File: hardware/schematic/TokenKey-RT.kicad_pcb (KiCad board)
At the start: 4 copper layers, 50 x 40 mm, 103 parts, among them J1 USB-C, J2 Header 1x04 P2.54 H3.0 (OLED), J3 TC2030-NL, Q1 AO3401A, SW1 SW_BOOT, SW2 EC11E18244A5, SW3 BTN1, SW4 BTN2, U1 MIMXRT1062DVL6B, U2 AP2112K-3.3TRG1, U3 TLV62569DBVR, U4 W25Q64JVSSIQ, U5 APS6404L-3SQR-ZR, U6 USBLC6-2SC6, Y1 24MHz 12pF, Y2 32.768kHz 12.5pF

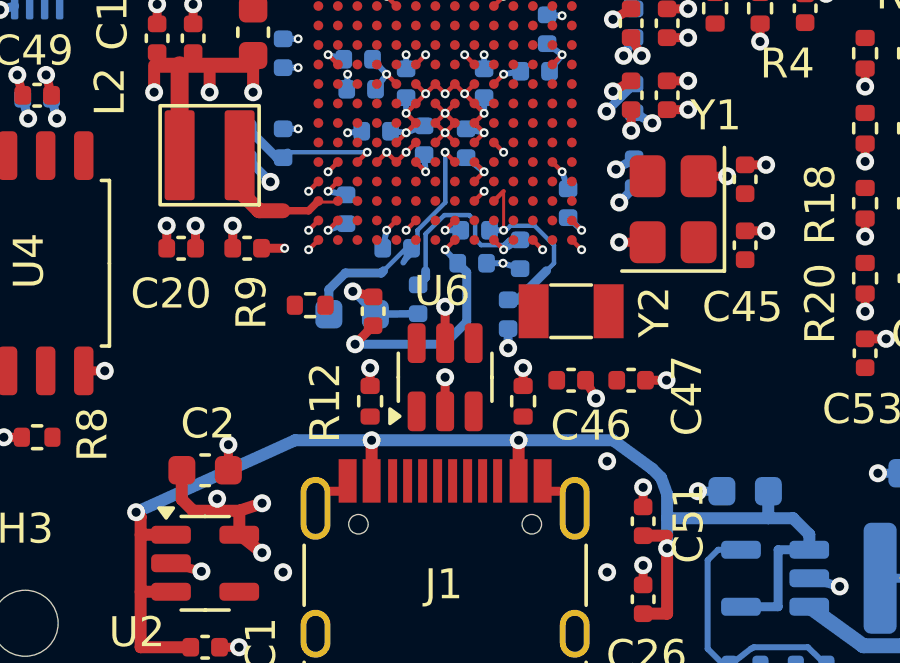
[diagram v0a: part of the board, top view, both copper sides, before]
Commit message: Route USB HS pair U1 -> USBLC6 -> J1 on L1 (Part of #58)
B-row J1 ties and diff-pair gap/uncoupled DRC errors remain open; see layout-notes §5.
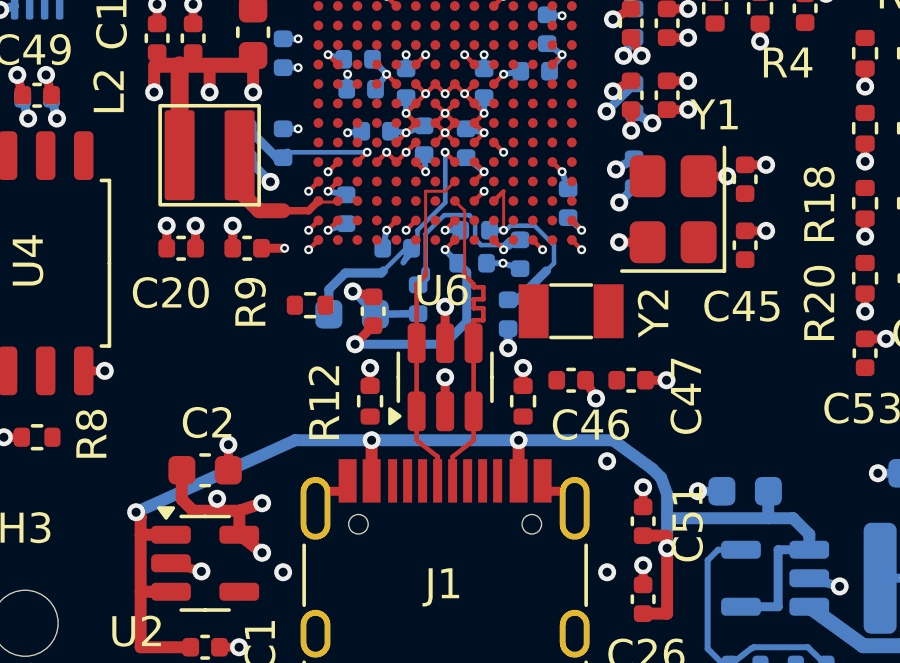
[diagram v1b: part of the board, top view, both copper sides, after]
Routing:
- net USB_DP: track 0.00 -> 11.2 mm
- net USB_DN: track 0.00 -> 11.2 mm
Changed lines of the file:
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@@
+	)
+	(segment
+		(start 16.05 30.4)
+		(end 16.05 30.9)
+		(width 0.155)
+		(layer "F.Cu")
+		(net 9)
+	)
+	(segment
+		(start 17 22.6)
+		(end 16.35 22.6)
+		(width 0.1)
+		(layer "F.Cu")
+		(net 9)
+	)
+	(segment
+		(start 16.05 30.9)
+		(end 16.75 31.45)
+		(width 0.155)
+		(layer "F.Cu")
+		(net 9)
+	)
+	(segment
+		(start 16.75 31.45)
+		(end 16.75 32.259999)
+		(width 0.155)
+		(layer "F.Cu")
+		(net 9)
+	)
+	(segment
+		(start 17.325 22.275)
+		(end 17 22.6)
+		(width 0.1)
+		(layer "F.Cu")
+		(net 9)
+	)
+	(segment
+		(start 16.35 22.6)
+		(end 16.35 25.275)
+		(width 0.1)
+		(layer "F.Cu")
+		(net 9)
+	)
+	(segment
+		(start 16.35 25.4)
+		(end 16.05 25.7)
+		(width 0.155)
+		(layer "F.Cu")
+		(net 9)
+	)
+	(segment
+		(start 16.05 25.7)
+		(end 16.05 30.4)
+		(width 0.155)
+		(layer "F.Cu")
+		(net 9)
+	)
+	(segment
+		(start 16.35 25.275)
+		(end 16.35 25.4)
+		(width 0.155)
+		(layer "F.Cu")
+		(net 9)
 	)
 	(segment
@@
 	)
 	(segment
+		(start 17.95 25.7)
+		(end 17.95 25.8)
+		(width 0.155)
+		(layer "F.Cu")
+		(net 33)
+	)
+	(segment
+		(start 17.65 23.25)
+		(end 17.65 25.275)
+		(width 0.1)
+		(layer "F.Cu")
+		(net 33)
+	)
+	(segment
+		(start 17.95 30.9)
+		(end 17.25 31.45)
+		(width 0.155)
+		(layer "F.Cu")
+		(net 33)
+	)
+	(segment
+		(start 17.95 26.2)
+		(end 17.95 26.5)
+		(width 0.155)
+		(layer "F.Cu")
+		(net 33)
+	)
+	(segment
+		(start 17.95 25.8)
+		(end 18.275 25.8)
+		(width 0.155)
+		(layer "F.Cu")
+		(net 33)
+	)
+	(segment
+		(start 17.95 26.5)
+		(end 18.275 26.5)
+		(width 0.155)
+		(layer "F.Cu")
+		(net 33)
+	)
+	(segment
+		(start 17.325 22.925)
+		(end 17.65 23.25)
+		(width 0.1)
+		(layer "F.Cu")
+		(net 33)
+	)
+	(segment
+		(start 18.275 25.8)
+		(end 18.275 26.2)
+		(width 0.155)
+		(layer "F.Cu")
+		(net 33)
+	)
+	(segment
+		(start 17.95 30.4)
+		(end 17.95 30.9)
+		(width 0.155)
+		(layer "F.Cu")
+		(net 33)
+	)
+	(segment
+		(start 18.275 26.2)
+		(end 17.95 26.2)
+		(width 0.155)
+		(layer "F.Cu")
+		(net 33)
+	)
+	(segment
+		(start 18.275 26.9)
+		(end 17.95 26.9)
+		(width 0.155)
+		(layer "F.Cu")
+		(net 33)
+	)
+	(segment
+		(start 17.25 31.45)
+		(end 17.25 32.259999)
+		(width 0.155)
+		(layer "F.Cu")
+		(net 33)
+	)
+	(segment
+		(start 17.65 25.4)
+		(end 17.95 25.7)
+		(width 0.155)
+		(layer "F.Cu")
+		(net 33)
+	)
+	(segment
+		(start 17.65 25.275)
+		(end 17.65 25.4)
+		(width 0.155)
+		(layer "F.Cu")
+		(net 33)
+	)
+	(segment
+		(start 17.95 26.9)
+		(end 17.95 30.4)
+		(width 0.155)
+		(layer "F.Cu")
+		(net 33)
+	)
+	(segment
+		(start 18.275 26.5)
+		(end 18.275 26.9)
+		(width 0.155)
+		(layer "F.Cu")
+		(net 33)
+	)
+	(segment

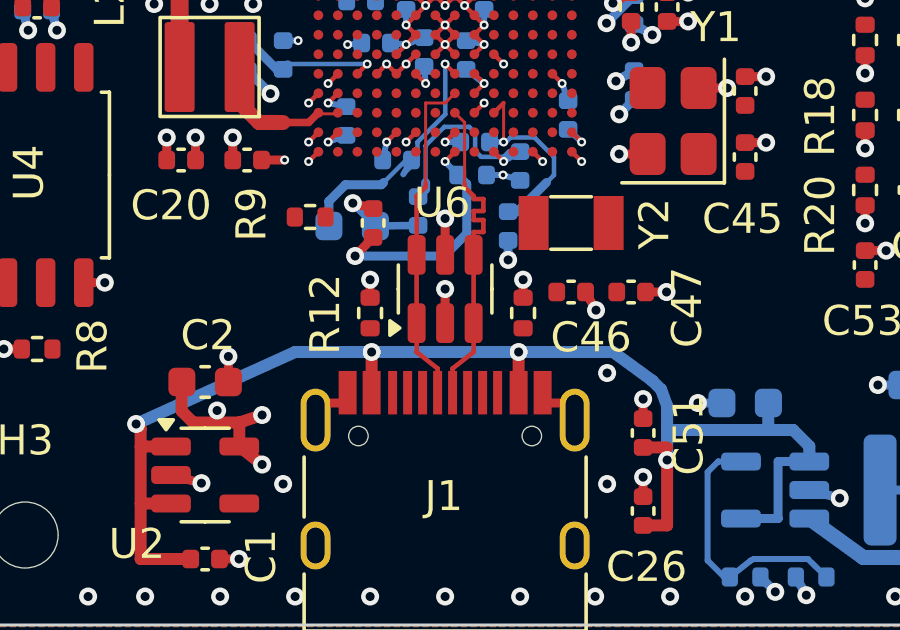
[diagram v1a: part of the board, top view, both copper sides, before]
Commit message: USB HS: J1 B-row via-in-pad ties, 45R uncoupled width, DRU exception
Fixes #58
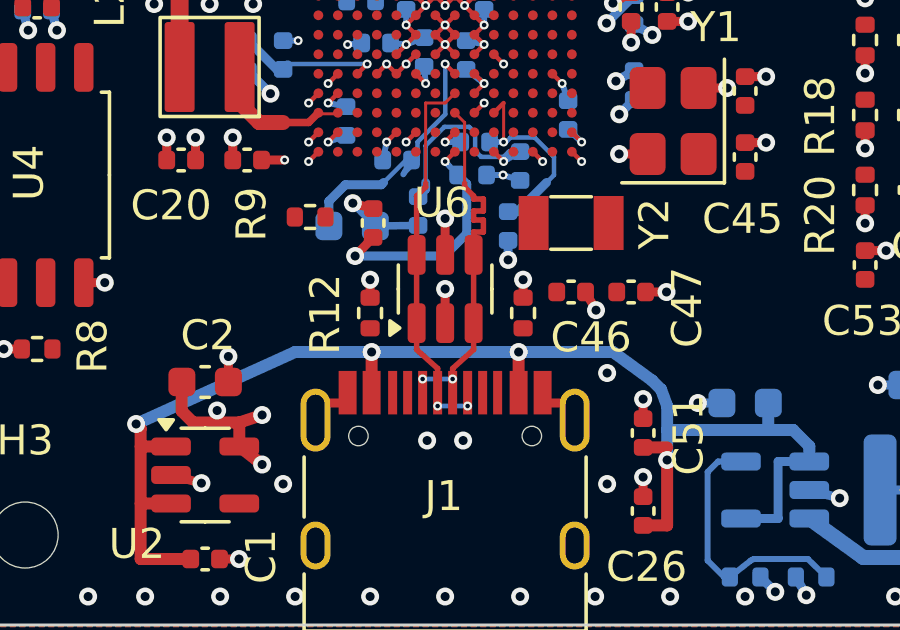
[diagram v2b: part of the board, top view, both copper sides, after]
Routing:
- net USB_DP: track 11.2 -> 12.2 mm, vias 0 -> 2
- net USB_DN: track 11.2 -> 12.2 mm, vias 0 -> 2
- net GND: vias 138 -> 140
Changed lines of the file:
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@@
 	)
 	(segment
-		(start 16.05 30.4)
-		(end 16.05 30.9)
-		(width 0.155)
+		(start 16.05 30.82)
+		(end 16.75 31.45)
+		(width 0.185)
 		(layer "F.Cu")
 		(net 9)
@@
 	)
 	(segment
-		(start 16.05 30.9)
-		(end 16.75 31.45)
-		(width 0.155)
-		(layer "F.Cu")
-		(net 9)
-	)
-	(segment
 		(start 16.75 31.45)
 		(end 16.75 32.259999)
-		(width 0.155)
+		(width 0.185)
+		(layer "F.Cu")
+		(net 9)
+	)
+	(segment
+		(start 16.05 30.4)
+		(end 16.05 30.82)
+		(width 0.185)
 		(layer "F.Cu")
 		(net 9)
@@
 		(start 16.35 25.4)
 		(end 16.05 25.7)
-		(width 0.155)
+		(width 0.185)
 		(layer "F.Cu")
 		(net 9)
@@
 		(start 16.05 25.7)
 		(end 16.05 30.4)
-		(width 0.155)
+		(width 0.185)
 		(layer "F.Cu")
 		(net 9)
@@
 		(start 16.35 25.275)
 		(end 16.35 25.4)
+		(width 0.185)
+		(layer "F.Cu")
+		(net 9)
+	)
+	(via
+		(at 16.75 32.7)
+		(size 0.3)
+		(drill 0.15)
+		(layers "F.Cu" "B.Cu")
+		(tenting front back)
+		(net 9)
+	)
+	(via
+		(at 17.75 32.7)
+		(size 0.3)
+		(drill 0.15)
+		(layers "F.Cu" "B.Cu")
+		(tenting front back)
+		(net 9)
+	)
+	(segment
+		(start 16.75 32.7)
+		(end 17.75 32.7)
 		(width 0.155)
-		(layer "F.Cu")
+		(layer "B.Cu")
 		(net 9)
 	)
@@
 	)
 	(via
+		(at 16.399999 33.85)
+		(size 0.6)
+		(drill 0.3)
+		(layers "F.Cu" "B.Cu")
+		(net 29)
+	)
+	(via
 		(at 0.95 12.5)
 		(size 0.6)
@@
 		(layers "F.Cu" "B.Cu")
 		(tenting front back)
+		(net 29)
+	)
+	(via
+		(at 17.6 33.85)
+		(size 0.6)
+		(drill 0.3)
+		(layers "F.Cu" "B.Cu")
 		(net 29)
 	)
@@
 		(start 17.95 25.7)
 		(end 17.95 25.8)
-		(width 0.155)
+		(width 0.185)
 		(layer "F.Cu")
 		(net 33)
@@
 	)
 	(segment
-		(start 17.95 30.9)
-		(end 17.25 31.45)
-		(width 0.155)
-		(layer "F.Cu")
-		(net 33)
-	)
-	(segment
 		(start 17.95 26.2)
 		(end 17.95 26.5)
-		(width 0.155)
+		(width 0.185)
 		(layer "F.Cu")
 		(net 33)
@@
 		(start 17.95 25.8)
 		(end 18.275 25.8)
-		(width 0.155)
+		(width 0.185)
 		(layer "F.Cu")
 		(net 33)
@@
 		(start 17.95 26.5)
 		(end 18.275 26.5)
-		(width 0.155)
+		(width 0.185)
 		(layer "F.Cu")
 		(net 33)
@@
 		(start 18.275 25.8)
 		(end 18.275 26.2)
-		(width 0.155)
+		(width 0.185)
 		(layer "F.Cu")
 		(net 33)
 	)
 	(segment
-		(start 17.95 30.4)
-		(end 17.95 30.9)
-		(width 0.155)
+		(start 17.95 30.82)
+		(end 17.25 31.45)
+		(width 0.185)
 		(layer "F.Cu")
 		(net 33)
@@
 		(start 18.275 26.2)
 		(end 17.95 26.2)
-		(width 0.155)
+		(width 0.185)
 		(layer "F.Cu")
 		(net 33)
@@
 		(start 18.275 26.9)
 		(end 17.95 26.9)
-		(width 0.155)
+		(width 0.185)
 		(layer "F.Cu")
 		(net 33)
@@
 		(start 17.25 31.45)
 		(end 17.25 32.259999)
-		(width 0.155)
+		(width 0.185)
 		(layer "F.Cu")
 		(net 33)
@@
 		(start 17.65 25.4)
 		(end 17.95 25.7)
-		(width 0.155)
+		(width 0.185)
+		(layer "F.Cu")
+		(net 33)
+	)
+	(segment
+		(start 17.95 30.4)
+		(end 17.95 30.82)
+		(width 0.185)
 		(layer "F.Cu")
 		(net 33)
@@
 		(start 17.65 25.275)
 		(end 17.65 25.4)
-		(width 0.155)
+		(width 0.185)
 		(layer "F.Cu")
 		(net 33)
@@
 		(start 17.95 26.9)
 		(end 17.95 30.4)
-		(width 0.155)
+		(width 0.185)
 		(layer "F.Cu")
 		(net 33)
@@
 		(start 18.275 26.5)
 		(end 18.275 26.9)
+		(width 0.185)
+		(layer "F.Cu")
+		(net 33)
+	)
+	(via
+		(at 16.25 31.8)
+		(size 0.3)
+		(drill 0.15)
+		(layers "F.Cu" "B.Cu")
+		(tenting front back)
+		(net 33)
+	)
+	(via
+		(at 17.25 31.8)
+		(size 0.3)
+		(drill 0.15)
+		(layers "F.Cu" "B.Cu")
+		(tenting front back)
+		(net 33)
+	)
+	(segment
+		(start 16.25 31.8)
+		(end 17.25 31.8)
 		(width 0.155)
-		(layer "F.Cu")
+		(layer "B.Cu")
 		(net 33)
 	)

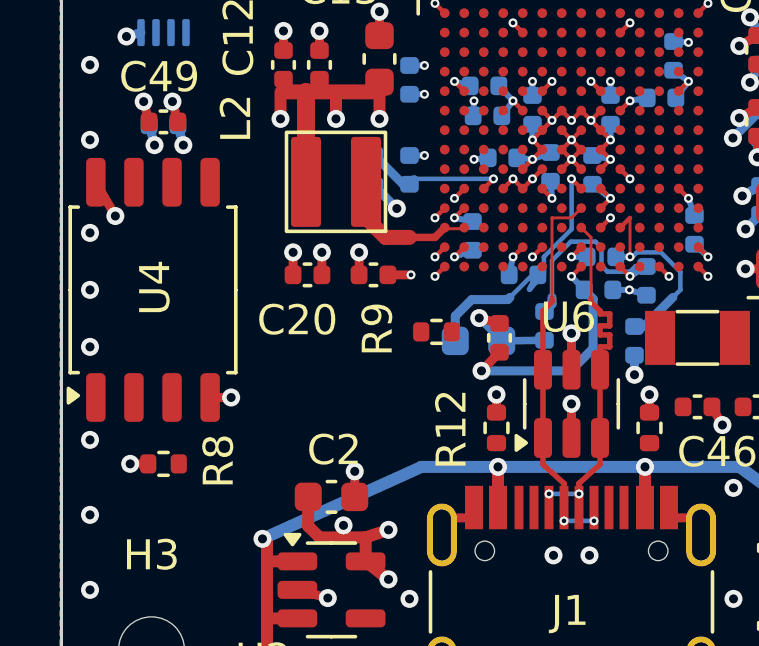
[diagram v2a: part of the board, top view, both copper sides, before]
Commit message: Route QSPI flash nets (CS/SCLK/IO0-3) to U4, length-matched
Fixes #59
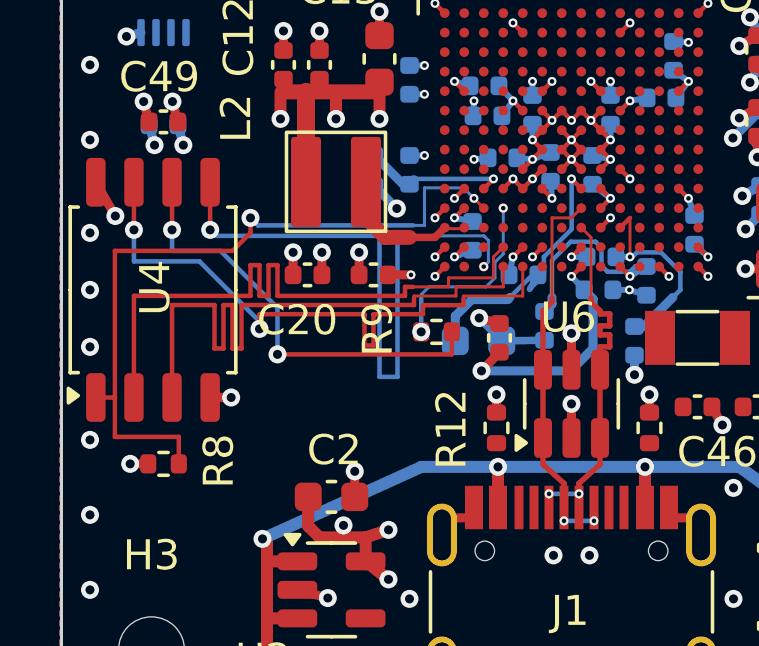
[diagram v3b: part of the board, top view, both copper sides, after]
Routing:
- net FLASH_CS: track 0.00 -> 24.5 mm, vias 0 -> 2
- net FLASH_IO0: track 0.00 -> 21.3 mm, vias 0 -> 2
- net FLASH_IO1: track 0.00 -> 21.2 mm
- net FLASH_IO2: track 0.00 -> 21.2 mm
- net FLASH_IO3: track 0.00 -> 20.8 mm, vias 0 -> 2
- net FLASH_CLK: track 0.00 -> 14.7 mm, vias 0 -> 2
- net QSPIA_SCLK: track 0.00 -> 6.37 mm, vias 0 -> 2

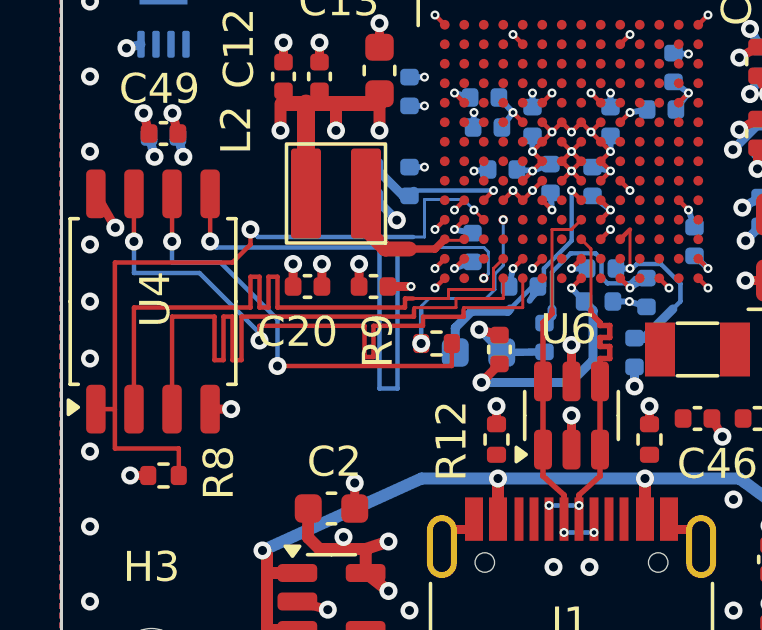
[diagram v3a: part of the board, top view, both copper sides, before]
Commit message: QSPI: move R9 pad-1 via-in-pad to off-pad dog-bone (DFM), keep SCLK match
Part of #60
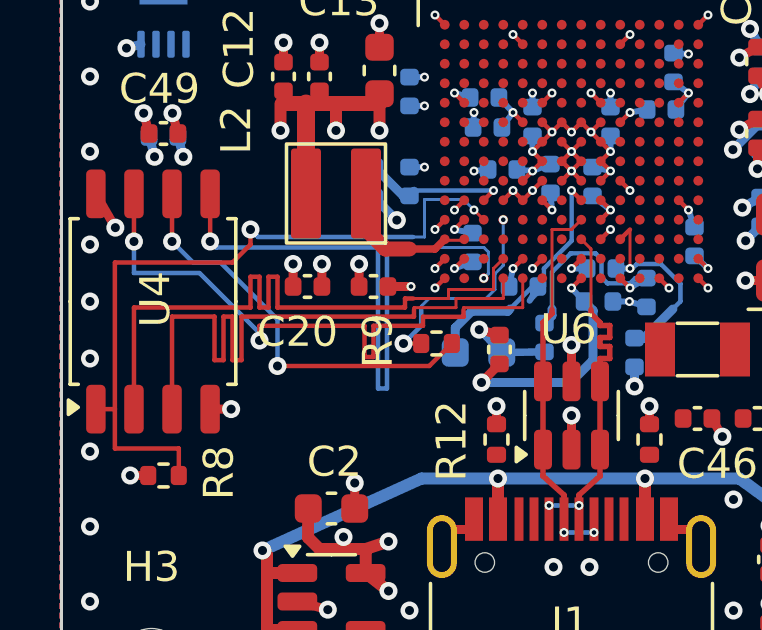
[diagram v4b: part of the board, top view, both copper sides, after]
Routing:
- net FLASH_CLK: track 14.7 -> 13.9 mm
- net QSPIA_SCLK: track 6.37 -> 7.21 mm
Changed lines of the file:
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@@
 	)
 	(segment
-		(start 11.2 23.2)
-		(end 11.2 27.9)
+		(start 10.85 27.9)
+		(end 10.55 27.9)
 		(width 0.15)
 		(layer "B.Cu")
@@
 	)
 	(segment
-		(start 10.6 27.9)
-		(end 10.6 23.2)
+		(start 10.55 27.9)
+		(end 10.55 23.2)
 		(width 0.15)
 		(layer "B.Cu")
@@
 	)
 	(segment
-		(start 10.6 23.2)
-		(end 5.155 23.2)
+		(start 11.725 23.2)
+		(end 10.85 23.2)
 		(width 0.15)
 		(layer "B.Cu")
@@
 	)
 	(segment
-		(start 11.725 23.2)
-		(end 11.2 23.2)
+		(start 10.55 23.2)
+		(end 5.155 23.2)
 		(width 0.15)
 		(layer "B.Cu")
@@
 	)
 	(segment
-		(start 11.2 27.9)
-		(end 10.6 27.9)
-		(width 0.15)
+		(start 14.08 23.2)
+		(end 11.725 23.2)
+		(width 0.1)
 		(layer "B.Cu")
 		(net 5)
 	)
 	(segment
-		(start 14.08 23.2)
-		(end 11.725 23.2)
-		(width 0.1)
+		(start 10.85 23.2)
+		(end 10.85 27.9)
+		(width 0.15)
 		(layer "B.Cu")
 		(net 5)
@@
 	)
 	(segment
-		(start 5.7 23.7)
-		(end 1.78 23.7)
-		(width 0.15)
-		(layer "F.Cu")
-		(net 21)
-	)
-	(segment
 		(start 14.075 22.275)
 		(end 13.75 21.95)
@@
 		(net 21)
 	)
+	(segment
+		(start 5.7 23.7)
+		(end 1.78 23.7)
+		(width 0.15)
+		(layer "F.Cu")
+		(net 21)
+	)
 	(via
 		(at 13.75 21.95)
@@
 	)
 	(segment
-		(start 3.685 23)
-		(end 3.685 21.4125)
+		(start 13.01 26.4)
+		(end 12.26 27.15)
 		(width 0.15)
 		(layer "F.Cu")
@@
 	)
 	(segment
-		(start 13.01 27.15)
-		(end 7.2 27.15)
+		(start 3.685 23)
+		(end 3.685 21.4125)
 		(width 0.15)
 		(layer "F.Cu")
@@
 	)
 	(segment
-		(start 13.01 26.4)
-		(end 13.01 27.15)
+		(start 12.26 27.15)
+		(end 7.2 27.15)
 		(width 0.15)
 		(layer "F.Cu")
@@
 	)
 	(segment
-		(start 7.2 25.6)
-		(end 5.3 23.7)
+		(start 4.385 23.7)
+		(end 3.685 23)
 		(width 0.15)
 		(layer "B.Cu")
@@
 	(segment
 		(start 5.3 23.7)
-		(end 3.685 23.7)
+		(end 4.385 23.7)
 		(width 0.15)
 		(layer "B.Cu")
@@
 	)
 	(segment
-		(start 3.685 23.7)
-		(end 3.685 23)
+		(start 7.2 25.6)
+		(end 5.3 23.7)
 		(width 0.15)
 		(layer "B.Cu")
@@
 		(net 47)
 	)
+	(segment
+		(start 11.4 26.4)
+		(end 11.99 26.4)
+		(width 0.15)
+		(layer "F.Cu")
+		(net 48)
+	)
 	(via
 		(at 14.725 22.275)
@@
 	)
 	(via
-		(at 11.99 26.4)
+		(at 11.4 26.4)
 		(size 0.6)
 		(drill 0.3)
@@
 	)
 	(segment
-		(start 14.45 24.6)
-		(end 14.15 24.9)
-		(width 0.1)
+		(start 11.99 25.81)
+		(end 11.4 26.4)
+		(width 0.15)
 		(layer "B.Cu")
 		(net 48)
 	)
 	(segment
-		(start 11.99 25.275)
-		(end 11.99 26.4)
-		(width 0.15)
+		(start 14.45 24.6)
+		(end 14.15 24.9)
+		(width 0.1)
 		(layer "B.Cu")
 		(net 48)
@@
 	)
 	(segment
+		(start 11.99 25.76)
+		(end 11.99 25.81)
+		(width 0.15)
+		(layer "B.Cu")
+		(net 48)
+	)
+	(segment
 		(start 14.725 22.275)
 		(end 14.725 23.8)
@@
 		(layer "B.Cu")
 		(net 48)
+	)
+	(segment
+		(start 11.99 25.275)
+		(end 11.99 25.76)
+		(width 0.15)
+		(layer "B.Cu")
+		(net 48)

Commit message: Route UART_TX/RX to TP1/TP2 and BOOT_MODE1 G14 to Q1 (connector; BGA via size/tent via pcbnew)
Part of #60
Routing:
- net UART_RX: track 0.00 -> 17.4 mm, vias 0 -> 3
- net UART_TX: track 0.00 -> 13.8 mm, vias 0 -> 1
- net BOOT_MODE1: track 0.00 -> 10.1 mm
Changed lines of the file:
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@@
 	)
 	(segment
+		(start 22.1 15.925)
+		(end 22.275 15.75)
+		(width 0.1)
+		(layer "F.Cu")
+		(net 4)
+	)
+	(segment
+		(start 25.825 12.2)
+		(end 26.5625 12.05)
+		(width 0.15)
+		(layer "F.Cu")
+		(net 4)
+	)
+	(segment
+		(start 22.1 18.65)
+		(end 22.1 15.925)
+		(width 0.1)
+		(layer "F.Cu")
+		(net 4)
+	)
+	(segment
+		(start 21.25 19.5)
+		(end 22.1 18.65)
+		(width 0.1)
+		(layer "F.Cu")
+		(net 4)
+	)
+	(segment
+		(start 22.275 15.75)
+		(end 23.3 14.725)
+		(width 0.15)
+		(layer "F.Cu")
+		(net 4)
+	)
+	(segment
+		(start 21.225 19.675)
+		(end 21.25 19.5)
+		(width 0.1)
+		(layer "F.Cu")
+		(net 4)
+	)
+	(segment
+		(start 23.3 14.725)
+		(end 25.825 12.2)
+		(width 0.15)
+		(layer "F.Cu")
+		(net 4)
+	)
+	(segment
 		(start 4.955 23)
 		(end 4.955 21.4125)
@@
 	)
 	(segment
+		(start 26.2 10.175)
+		(end 27.475 10.175)
+		(width 0.15)
+		(layer "F.Cu")
+		(net 22)
+	)
+	(segment
+		(start 21.225 22.275)
+		(end 21.325 22.15)
+		(width 0.1)
+		(layer "F.Cu")
+		(net 22)
+	)
+	(segment
+		(start 21.325 22.15)
+		(end 21.5 21.975)
+		(width 0.1)
+		(layer "F.Cu")
+		(net 22)
+	)
+	(segment
+		(start 22.275 14.1)
+		(end 26.2 10.175)
+		(width 0.15)
+		(layer "F.Cu")
+		(net 22)
+	)
+	(segment
+		(start 21 15.375)
+		(end 21.65 14.725)
+		(width 0.1)
+		(layer "F.Cu")
+		(net 22)
+	)
+	(segment
+		(start 21.65 14.725)
+		(end 22.275 14.1)
+		(width 0.15)
+		(layer "F.Cu")
+		(net 22)
+	)
+	(via
+		(at 27.475 10.175)
+		(size 0.6)
+		(drill 0.3)
+		(layers "F.Cu" "B.Cu")
+		(tenting front back)
+		(net 22)
+	)
+	(via
+		(at 21.5 21.975)
+		(size 0.3)
+		(drill 0.15)
+		(layers "F.Cu" "B.Cu")
+		(tenting front back)
+		(net 22)
+	)
+	(via
+		(at 21 15.375)
+		(size 0.3)
+		(drill 0.15)
+		(layers "F.Cu" "B.Cu")
+		(tenting front back)
+		(net 22)
+	)
+	(segment
+		(start 21.5 15.875)
+		(end 21 15.375)
+		(width 0.1)
+		(layer "B.Cu")
+		(net 22)
+	)
+	(segment
+		(start 21.5 21.975)
+		(end 21.5 15.875)
+		(width 0.1)
+		(layer "B.Cu")
+		(net 22)
+	)
+	(segment
+		(start 27.475 10.175)
+		(end 28.525 10.175)
+		(width 0.15)
+		(layer "B.Cu")
+		(net 22)
+	)
+	(segment
+		(start 28.525 10.175)
+		(end 29 10)
+		(width 0.15)
+		(layer "B.Cu")
+		(net 22)
+	)
+	(segment
 		(start 9.775 31.9)
 		(end 9.775 31.05)
@@
 	)
 	(segment
+		(start 21.25 21.45)
+		(end 21.9 20.8)
+		(width 0.1)
+		(layer "F.Cu")
+		(net 36)
+	)
+	(segment
+		(start 21.225 21.625)
+		(end 21.25 21.45)
+		(width 0.1)
+		(layer "F.Cu")
+		(net 36)
+	)
+	(via
+		(at 21.9 20.8)
+		(size 0.3)
+		(drill 0.15)
+		(layers "F.Cu" "B.Cu")
+		(tenting front back)
+		(net 36)
+	)
+	(segment
+		(start 22.275 14.475)
+		(end 26.3 10.45)
+		(width 0.15)
+		(layer "B.Cu")
+		(net 36)
+	)
+	(segment
+		(start 22.025 14.725)
+		(end 22.275 14.475)
+		(width 0.15)
+		(layer "B.Cu")
+		(net 36)
+	)
+	(segment
+		(start 26.3 10.45)
+		(end 26.5 10)
+		(width 0.15)
+		(layer "B.Cu")
+		(net 36)
+	)
+	(segment
+		(start 21.9 14.85)
+		(end 22.025 14.725)
+		(width 0.1)
+		(layer "B.Cu")
+		(net 36)
+	)
+	(segment
+		(start 21.9 20.8)
+		(end 21.9 14.85)
+		(width 0.1)
+		(layer "B.Cu")
+		(net 36)
+	)
+	(segment
